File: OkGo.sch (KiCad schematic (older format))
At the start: 27 parts

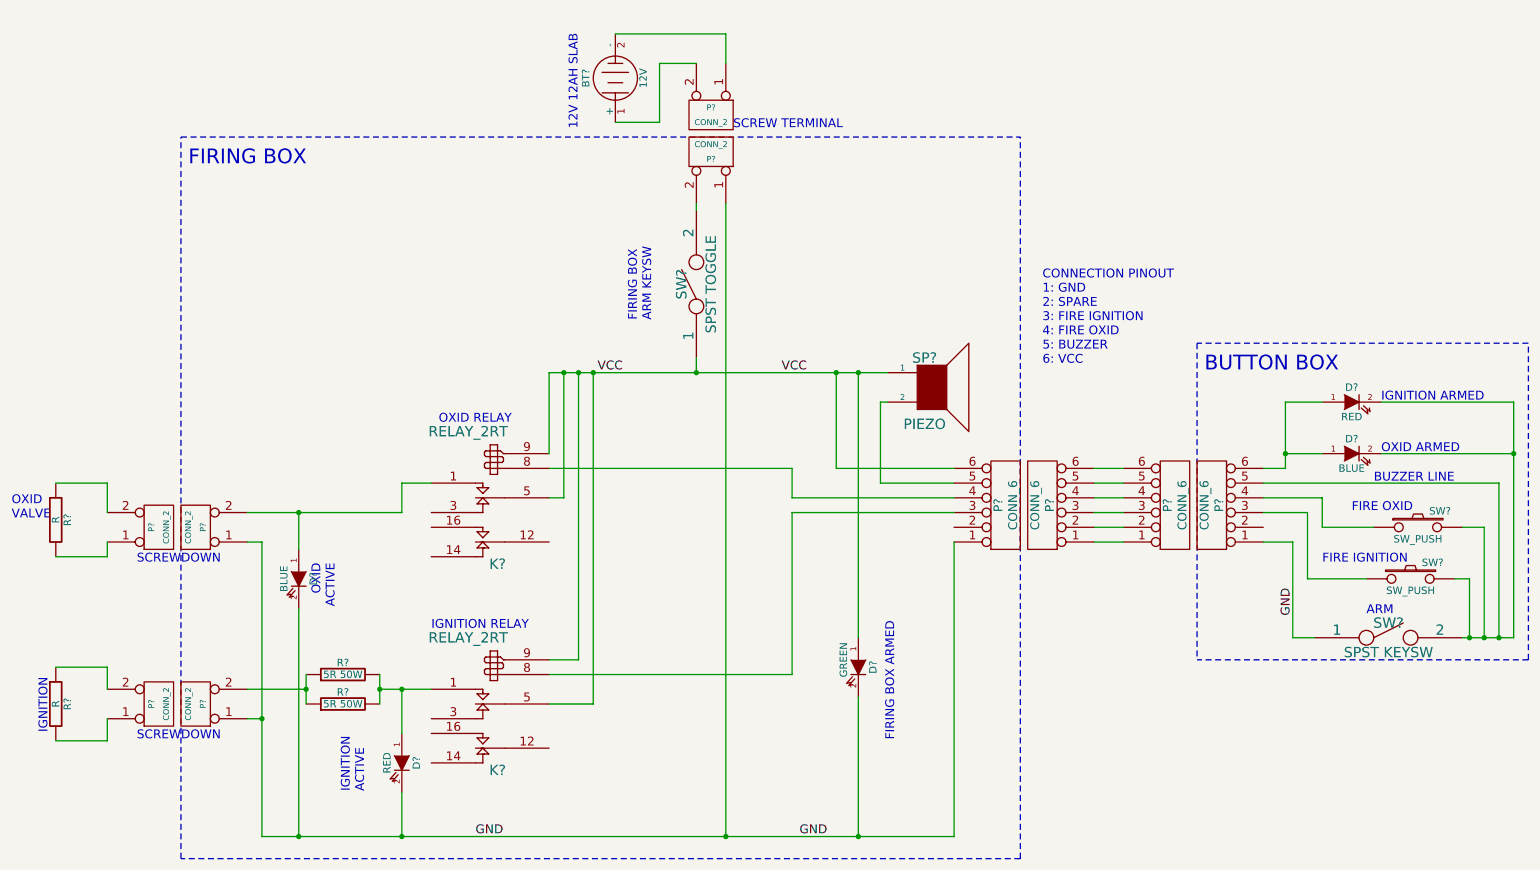
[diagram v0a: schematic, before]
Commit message: Added low oxid channel to schematic
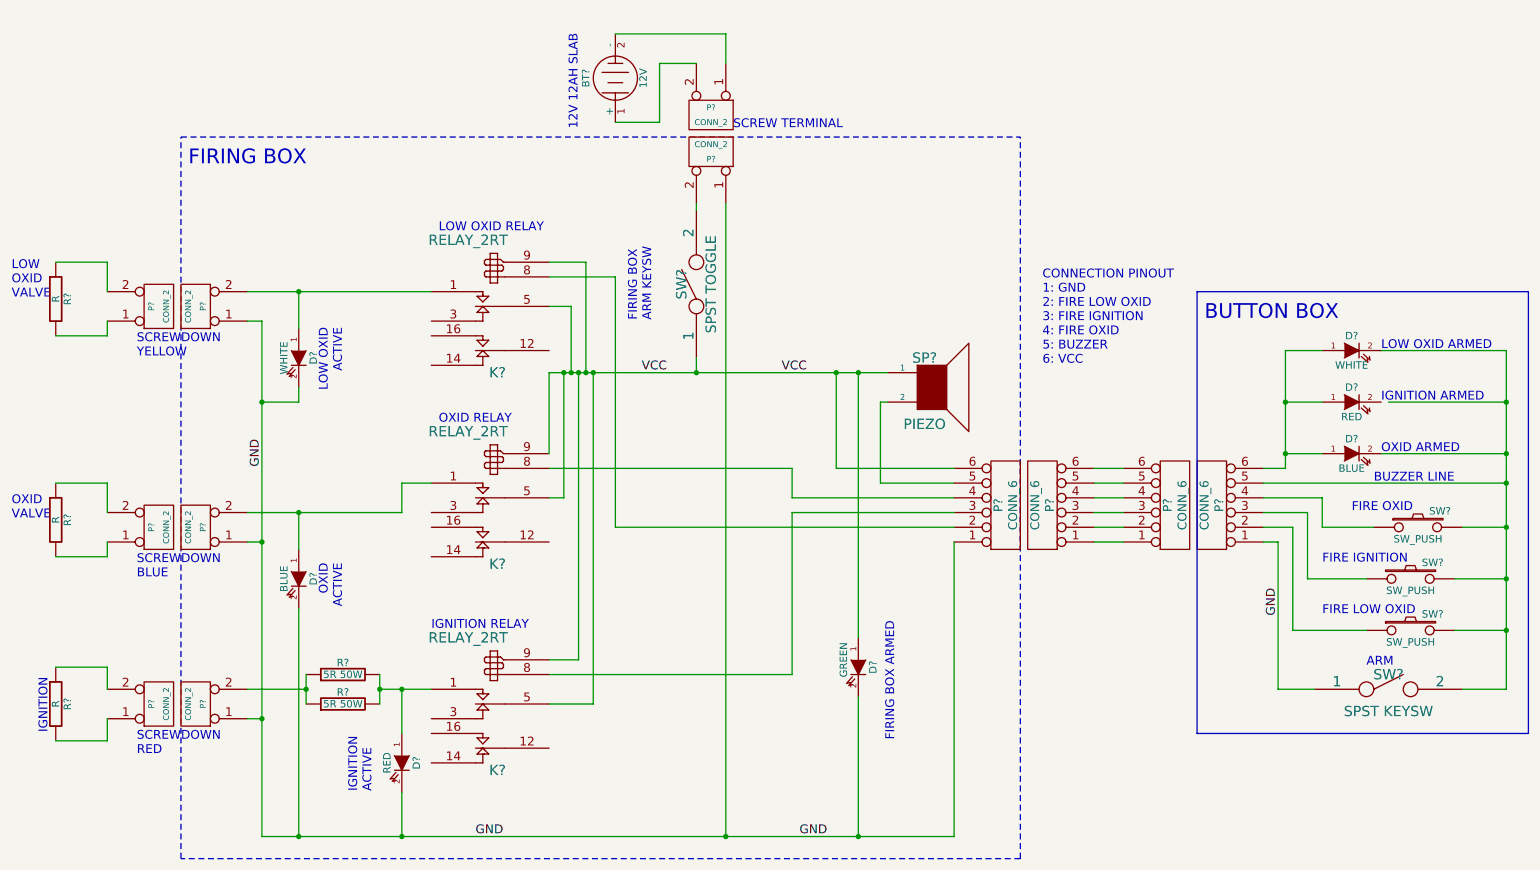
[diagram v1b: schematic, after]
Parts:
- added D?: WHITE, symbol LED
- added D?: RED, symbol LED
- added K?: RELAY_2RT, symbol RELAY_2RT
- added P? (x2): CONN_2, symbol CONN_2
- added R?: R, symbol R
- added SW?: SW_PUSH, symbol SW_PUSH
- D?: value RED -> WHITE
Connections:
- net GND: now also D?.2 (K), P?.1 (P1)
- net VCC: now also K?.5 (C1), K?.9
- net at D?.2 (K), D?.2 (K), P?.5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: now also SW?.2
- net at D?.1 (A), D?.1 (A), P?.6: now also D?.1 (A)
- net at P?.2: now also K?.8
- net at P?.2: now also SW?.1
- new net: D?.1 (A), K?.1 (T1), P?.2 (PM)
- new net: P?.1 (P1), R?.2
- new net: P?.2 (PM), R?.1
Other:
- note added: "CONNECTION PINOUT\n1: GND\n2: FIRE LOW OXID\n3: FIRE IGNITION\n4: FIRE OXID\n5: BUZZER\n6: VCC"
- note added: "FIRE LOW OXID"
- note added: "LOW OXID ARMED"
- note added: "LOW OXID RELAY"
- note added: "LOW OXID\nACTIVE"
- note added: "LOW\nOXID\nVALVE"
- note added: "SCREWDOWN\nBLUE"
- note added: "SCREWDOWN\nRED"
- note added: "SCREWDOWN\nYELLOW"
- note removed: "CONNECTION PINOUT\n1: GND\n2: SPARE\n3: FIRE IGNITION\n4: FIRE OXID\n5: BUZZER\n6: VCC"
- note removed: "SCREWDOWN"
- moved on the sheet: D?, SW?

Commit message: Annotated schematic
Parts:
- gave numbers to parts that had none: 34
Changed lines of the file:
@@
 SCREWDOWN\nRED
 $Comp
-L LED D?
+L LED D6
 U 1 1 50B2244A
 P 6300 4850
-F 0 "D?" H 6300 4950 50  0000 C CNN
+F 0 "D6" H 6300 4950 50  0000 C CNN
 F 1 "GREEN" H 6250 4750 50  0000 C CNN
 F 2 "" H 6300 4850 60  0001 C CNN
@@
 FIRING BOX
 $Comp
-L LED D?
+L LED D4
 U 1 1 50B2232B
 P 9650 3400
-F 0 "D?" H 9650 3500 50  0000 C CNN
+F 0 "D4" H 9650 3500 50  0000 C CNN
 F 1 "BLUE" H 9650 3300 50  0000 C CNN
 F 2 "" H 9650 3400 60  0001 C CNN
@@
 $EndComp
 $Comp
-L LED D?
+L LED D7
 U 1 1 50B222A9
 P 3200 5500
-F 0 "D?" H 3200 5600 50  0000 C CNN
+F 0 "D7" H 3200 5600 50  0000 C CNN
 F 1 "RED" H 3200 5400 50  0000 C CNN
 F 2 "" H 3200 5500 60  0001 C CNN
@@
 $EndComp
 $Comp
-L LED D?
+L LED D5
 U 1 1 50B2229C
 P 2500 4250
-F 0 "D?" H 2500 4350 50  0000 C CNN
+F 0 "D5" H 2500 4350 50  0000 C CNN
 F 1 "BLUE" H 2500 4150 50  0000 C CNN
 F 2 "" H 2500 4250 60  0001 C CNN
@@
 $EndComp
 $Comp
-L CONN_2 P?
+L CONN_2 P11
 U 1 1 50B2217D
 P 1550 5100
-F 0 "P?" V 1500 5100 40  0000 C CNN
+F 0 "P11" V 1500 5100 40  0000 C CNN
 F 1 "CONN_2" V 1600 5100 40  0000 C CNN
 F 2 "" H 1550 5100 60  0001 C CNN
@@
 $EndComp
 $Comp
-L CONN_2 P?
+L CONN_2 P9
 U 1 1 50B2217A
 P 1550 3900
-F 0 "P?" V 1500 3900 40  0000 C CNN
+F 0 "P9" V 1500 3900 40  0000 C CNN
 F 1 "CONN_2" V 1600 3900 40  0000 C CNN
 F 2 "" H 1550 3900 60  0001 C CNN
@@
 $EndComp
 $Comp
-L CONN_2 P?
+L CONN_2 P12
 U 1 1 50B22177
 P 1800 5100
-F 0 "P?" V 1750 5100 40  0000 C CNN
+F 0 "P12" V 1750 5100 40  0000 C CNN
 F 1 "CONN_2" V 1850 5100 40  0000 C CNN
 F 2 "" H 1800 5100 60  0001 C CNN
@@
 $EndComp
 $Comp
-L CONN_2 P?
+L CONN_2 P10
 U 1 1 50B22171
 P 1800 3900
-F 0 "P?" V 1750 3900 40  0000 C CNN
+F 0 "P10" V 1750 3900 40  0000 C CNN
 F 1 "CONN_2" V 1850 3900 40  0000 C CNN
 F 2 "" H 1800 3900 60  0001 C CNN
@@
 $EndComp
 $Comp
-L SPST SW?
+L SPST SW5
 U 1 1 50B21E62
 P 9900 5000
-F 0 "SW?" H 9900 5100 70  0000 C CNN
+F 0 "SW5" H 9900 5100 70  0000 C CNN
 F 1 "SPST KEYSW" H 9900 4850 70  0000 C CNN
 F 2 "" H 9900 5000 60  0001 C CNN
@@
 $EndComp
 $Comp
-L SPST SW?
+L SPST SW1
 U 1 1 50B21E5F
 P 5200 2250
-F 0 "SW?" H 5200 2350 70  0000 C CNN
+F 0 "SW1" H 5200 2350 70  0000 C CNN
 F 1 "SPST TOGGLE" H 5200 2150 70  0000 C CNN
 F 2 "" H 5200 2250 60  0001 C CNN
@@
 $EndComp
 $Comp
-L SW_PUSH SW?
+L SW_PUSH SW2
 U 1 1 50B21E58
 P 10100 3900
-F 0 "SW?" H 10250 4010 50  0000 C CNN
+F 0 "SW2" H 10250 4010 50  0000 C CNN
 F 1 "SW_PUSH" H 10100 3820 50  0000 C CNN
 F 2 "" H 10100 3900 60  0001 C CNN
@@
 $EndComp
 $Comp
-L SW_PUSH SW?
+L SW_PUSH SW3
 U 1 1 50B21E55
 P 10050 4250
-F 0 "SW?" H 10200 4360 50  0000 C CNN
+F 0 "SW3" H 10200 4360 50  0000 C CNN
 F 1 "SW_PUSH" H 10050 4170 50  0000 C CNN
 F 2 "" H 10050 4250 60  0001 C CNN
@@
 OXID\nVALVE
 $Comp
-L R R?
+L R R4
 U 1 1 50B219E4
 P 850 5100
-F 0 "R?" V 930 5100 50  0000 C CNN
+F 0 "R4" V 930 5100 50  0000 C CNN
 F 1 "R" V 850 5100 50  0000 C CNN
 F 2 "" H 850 5100 60  0001 C CNN
@@
 $EndComp
 $Comp
-L R R?
+L R R2
 U 1 1 50B219DE
 P 850 3850
-F 0 "R?" V 930 3850 50  0000 C CNN
+F 0 "R2" V 930 3850 50  0000 C CNN
 F 1 "R" V 850 3850 50  0000 C CNN
 F 2 "" H 850 3850 60  0001 C CNN
@@
 $EndComp
 $Comp
-L RELAY_2RT K?
+L RELAY_2RT K3
 U 1 1 50B219CD
 P 3800 5150
-F 0 "K?" H 3750 5550 70  0000 C CNN
+F 0 "K3" H 3750 5550 70  0000 C CNN
 F 1 "RELAY_2RT" H 3950 4650 70  0000 C CNN
 F 2 "" H 3800 5150 60  0001 C CNN
@@
 $EndComp
 $Comp
-L RELAY_2RT K?
+L RELAY_2RT K2
 U 1 1 50B219C6
 P 3800 3750
-F 0 "K?" H 3750 4150 70  0000 C CNN
+F 0 "K2" H 3750 4150 70  0000 C CNN
 F 1 "RELAY_2RT" H 3950 3250 70  0000 C CNN
 F 2 "" H 3800 3750 60  0001 C CNN
@@
 $EndComp
 $Comp
-L CONN_2 P?
+L CONN_2 P2
 U 1 1 50B21968
 P 5300 1350
-F 0 "P?" V 5250 1350 40  0000 C CNN
+F 0 "P2" V 5250 1350 40  0000 C CNN
 F 1 "CONN_2" V 5350 1350 40  0000 C CNN
 F 2 "" H 5300 1350 60  0001 C CNN
@@
 $EndComp
 $Comp
-L CONN_2 P?
+L CONN_2 P1
 U 1 1 50B21962
 P 5300 1100
-F 0 "P?" V 5250 1100 40  0000 C CNN
+F 0 "P1" V 5250 1100 40  0000 C CNN
 F 1 "CONN_2" V 5350 1100 40  0000 C CNN
 F 2 "" H 5300 1100 60  0001 C CNN
@@
 $EndComp
 $Comp
-L BATTERY BT?
+L BATTERY BT1
 U 1 1 50B2192F
 P 4650 850
-F 0 "BT?" H 4650 1050 50  0000 C CNN
+F 0 "BT1" H 4650 1050 50  0000 C CNN
 F 1 "12V" H 4650 660 50  0000 C CNN
 F 2 "" H 4650 850 60  0001 C CNN
@@
 $EndComp
 $Comp
-L CONN_6 P?
+L CONN_6 P5
 U 1 1 50B3A3B9
 P 7300 3750
-F 0 "P?" V 7250 3750 60  0000 C CNN
+F 0 "P5" V 7250 3750 60  0000 C CNN
 F 1 "CONN_6" V 7350 3750 60  0000 C CNN
 F 2 "" H 7300 3750 60  0001 C CNN
@@
 $EndComp
 $Comp
-L CONN_6 P?
+L CONN_6 P6
 U 1 1 50B3A3C8
 P 7550 3750
-F 0 "P?" V 7500 3750 60  0000 C CNN
+F 0 "P6" V 7500 3750 60  0000 C CNN
 F 1 "CONN_6" V 7600 3750 60  0000 C CNN
 F 2 "" H 7550 3750 60  0001 C CNN
@@
 $EndComp
 $Comp
-L CONN_6 P?
+L CONN_6 P8
 U 1 1 50B3A3D7
 P 8700 3750
-F 0 "P?" V 8650 3750 60  0000 C CNN
+F 0 "P8" V 8650 3750 60  0000 C CNN
 F 1 "CONN_6" V 8750 3750 60  0000 C CNN
 F 2 "" H 8700 3750 60  0001 C CNN
@@
 $EndComp
 $Comp
-L CONN_6 P?
+L CONN_6 P7
 U 1 1 50B3A3E6
 P 8450 3750
-F 0 "P?" V 8400 3750 60  0000 C CNN
+F 0 "P7" V 8400 3750 60  0000 C CNN
 F 1 "CONN_6" V 8500 3750 60  0000 C CNN
 F 2 "" H 8450 3750 60  0001 C CNN
@@
 BUZZER LINE
 $Comp
-L SPEAKER SP?
+L SPEAKER SP1
 U 1 1 50B3A9E8
 P 6800 2950
-F 0 "SP?" H 6750 3150 70  0000 C CNN
+F 0 "SP1" H 6750 3150 70  0000 C CNN
 F 1 "PIEZO" H 6750 2700 70  0000 C CNN
 F 2 "" H 6800 2950 60  0001 C CNN
@@
 IGNITION RELAY
 $Comp
-L LED D?
+L LED D1
 U 1 1 50B3AFF2
 P 9650 2700
-F 0 "D?" H 9650 2800 50  0000 C CNN
+F 0 "D1" H 9650 2800 50  0000 C CNN
 F 1 "WHITE" H 9650 2600 50  0000 C CNN
 F 2 "" H 9650 2700 60  0001 C CNN
@@
 12V 12AH SLAB
 $Comp
-L R R?
+L R R5
 U 1 1 50B3B242
 P 2800 5100
-F 0 "R?" V 2880 5100 50  0000 C CNN
+F 0 "R5" V 2880 5100 50  0000 C CNN
 F 1 "5R 50W" V 2800 5100 50  0000 C CNN
 F 2 "" H 2800 5100 60  0001 C CNN
@@
 $EndComp
 $Comp
-L R R?
+L R R3
 U 1 1 50B3B260
 P 2800 4900
-F 0 "R?" V 2880 4900 50  0000 C CNN
+F 0 "R3" V 2880 4900 50  0000 C CNN
 F 1 "5R 50W" V 2800 4900 50  0000 C CNN
 F 2 "" H 2800 4900 60  0001 C CNN
@@
 SCREW TERMINAL
 $Comp
-L RELAY_2RT K?
+L RELAY_2RT K1
 U 1 1 531FA39D
 P 3800 2450
-F 0 "K?" H 3750 2850 70  0000 C CNN
+F 0 "K1" H 3750 2850 70  0000 C CNN
 F 1 "RELAY_2RT" H 3950 1950 70  0000 C CNN
 F 2 "" H 3800 2450 60  0001 C CNN
@@
 SCREWDOWN\nYELLOW
 $Comp
-L LED D?
+L LED D2
 U 1 1 531FA412
 P 2500 2750
-F 0 "D?" H 2500 2850 50  0000 C CNN
+F 0 "D2" H 2500 2850 50  0000 C CNN
 F 1 "WHITE" H 2500 2650 50  0000 C CNN
 F 2 "" H 2500 2750 60  0001 C CNN
@@
 $EndComp
 $Comp
-L CONN_2 P?
+L CONN_2 P3
 U 1 1 531FA418
 P 1550 2400
-F 0 "P?" V 1500 2400 40  0000 C CNN
+F 0 "P3" V 1500 2400 40  0000 C CNN
 F 1 "CONN_2" V 1600 2400 40  0000 C CNN
 F 2 "" H 1550 2400 60  0001 C CNN
@@
 $EndComp
 $Comp
-L CONN_2 P?
+L CONN_2 P4
 U 1 1 531FA41E
 P 1800 2400
-F 0 "P?" V 1750 2400 40  0000 C CNN
+F 0 "P4" V 1750 2400 40  0000 C CNN
 F 1 "CONN_2" V 1850 2400 40  0000 C CNN
 F 2 "" H 1800 2400 60  0001 C CNN
@@
 LOW\nOXID\nVALVE
 $Comp
-L R R?
+L R R1
 U 1 1 531FA425
 P 850 2350
-F 0 "R?" V 930 2350 50  0000 C CNN
+F 0 "R1" V 930 2350 50  0000 C CNN
 F 1 "R" V 850 2350 50  0000 C CNN
 F 2 "" H 850 2350 60  0001 C CNN
@@
 	9450 3050 9200 3050
 $Comp
-L LED D?
+L LED D3
 U 1 1 531FAAB3
 P 9650 3050
-F 0 "D?" H 9650 3150 50  0000 C CNN
+F 0 "D3" H 9650 3150 50  0000 C CNN
 F 1 "RED" H 9650 2950 50  0000 C CNN
 F 2 "" H 9650 3050 60  0001 C CNN
@@
 FIRE LOW OXID
 $Comp
-L SW_PUSH SW?
+L SW_PUSH SW4
 U 1 1 531FAD70
 P 10050 4600
-F 0 "SW?" H 10200 4710 50  0000 C CNN
+F 0 "SW4" H 10200 4710 50  0000 C CNN
 F 1 "SW_PUSH" H 10050 4520 50  0000 C CNN
 F 2 "" H 10050 4600 60  0001 C CNN

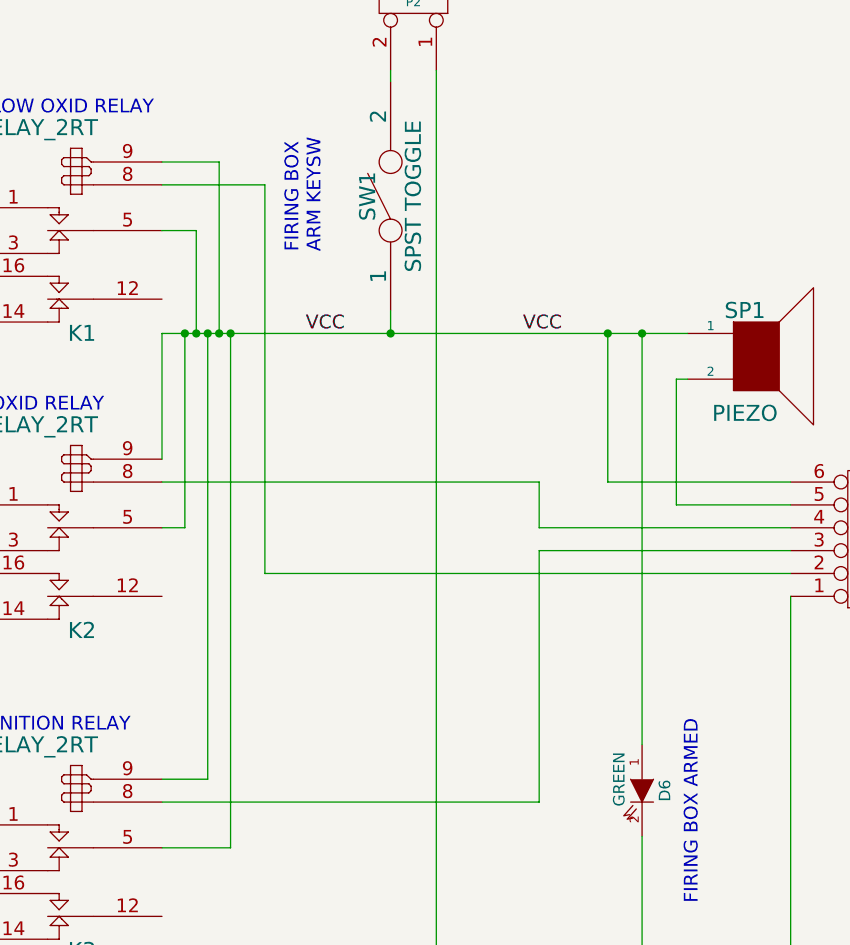
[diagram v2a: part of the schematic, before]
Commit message: New wiring layout on relay coils
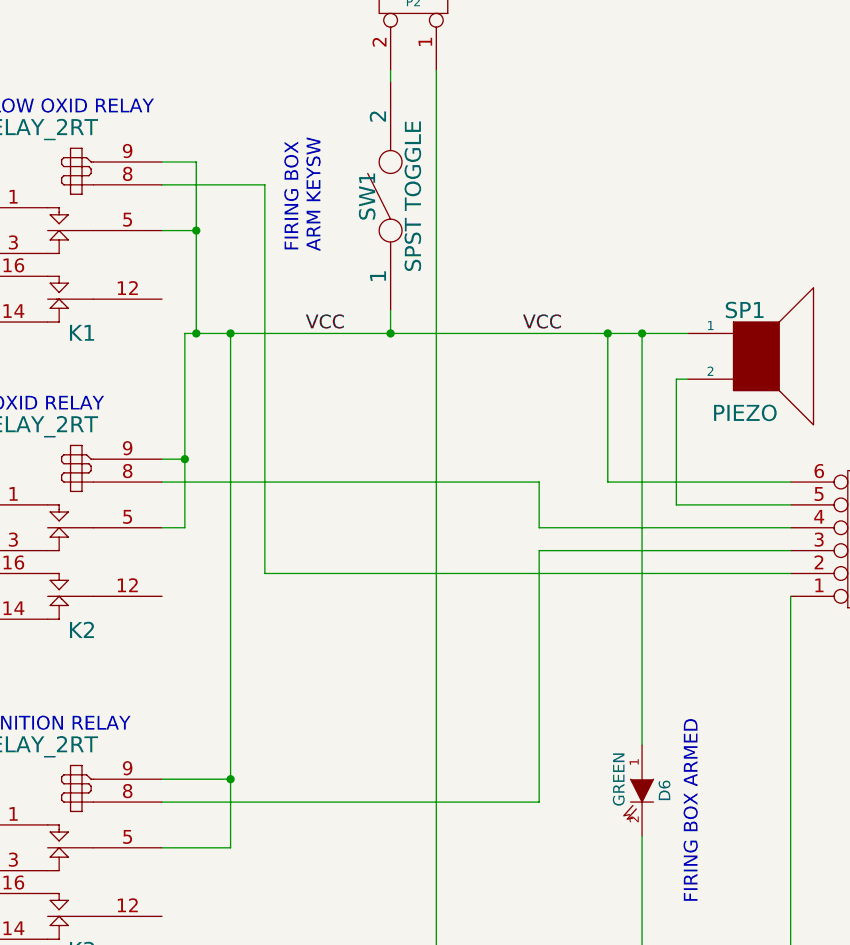
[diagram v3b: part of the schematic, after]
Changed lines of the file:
@@
 Wire Wire Line
 	6150 3500 6950 3500
-Connection ~ 4400 2850
-Wire Wire Line
-	4400 2850 4400 4800
-Wire Wire Line
-	4400 4800 4200 4800
 Connection ~ 6300 2850
 Wire Wire Line
 	6300 2850 6300 4650
-Connection ~ 4300 2850
 Wire Wire Line
 	4300 2850 4300 3700
@@
 Wire Wire Line
 	6950 3600 6450 3600
-Wire Wire Line
-	4200 2850 6500 2850
 Wire Wire Line
 	5400 750  5400 550
@@
 Wire Wire Line
 	5200 2850 5200 2750
-Wire Wire Line
-	4200 2850 4200 3400
 Wire Wire Line
 	6450 3600 6450 3050
@@
 	1    0    0    -1
 $EndComp
-Connection ~ 4450 2850
 Wire Wire Line
 	4650 3900 6950 3900
@@
 	4650 2200 4200 2200
 Wire Wire Line
-	4450 2850 4450 2100
-Wire Wire Line
-	4450 2100 4200 2100
-Wire Wire Line
 	4200 2400 4350 2400
 Wire Wire Line
-	4350 2400 4350 2850
+	4350 2100 4350 2850
 Connection ~ 4350 2850
 Wire Wire Line
@@
 Wire Bus Line
 	10850 2300 8600 2300
+Wire Wire Line
+	4200 2100 4350 2100
+Connection ~ 4350 2400
+Wire Wire Line
+	6500 2850 4300 2850
+Wire Wire Line
+	4200 3400 4300 3400
+Connection ~ 4300 3400
+Wire Wire Line
+	4200 4800 4500 4800
+Connection ~ 4500 4800
 $EndSCHEMATC
